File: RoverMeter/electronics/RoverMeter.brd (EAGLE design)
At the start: 35.6 x 14 mm, 17 parts, among them IC1 INA168, IC3 TINY85, J1 AVRISP, U1 MCP1824

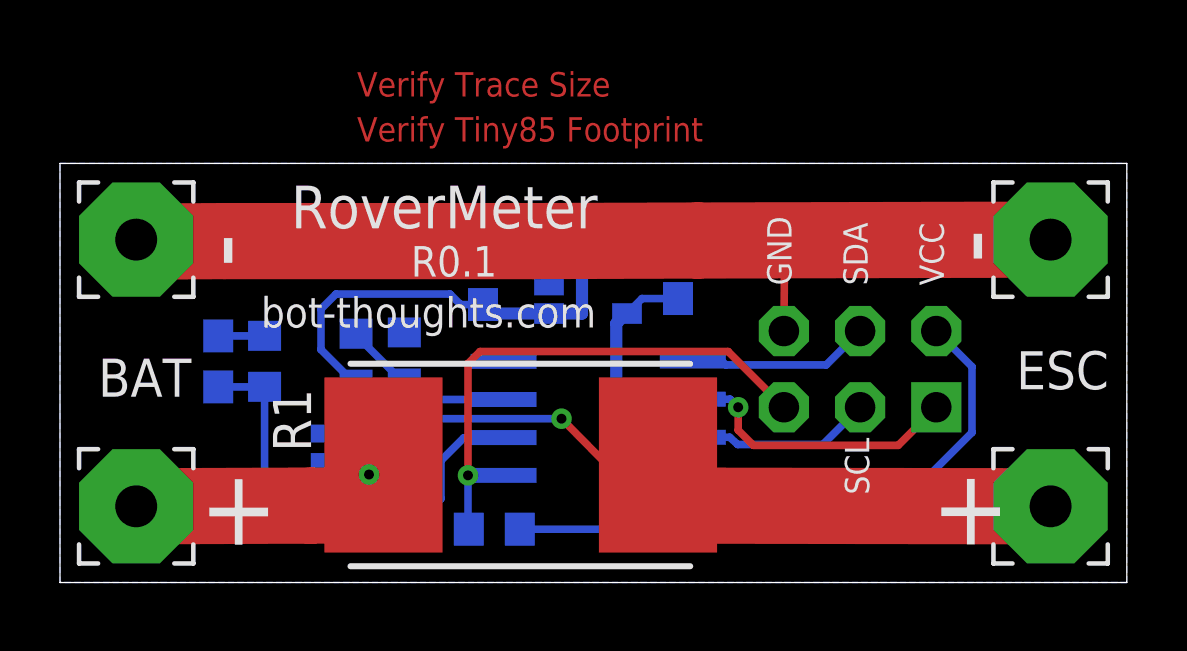
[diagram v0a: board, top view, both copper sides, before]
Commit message: Revised board layout somewhat
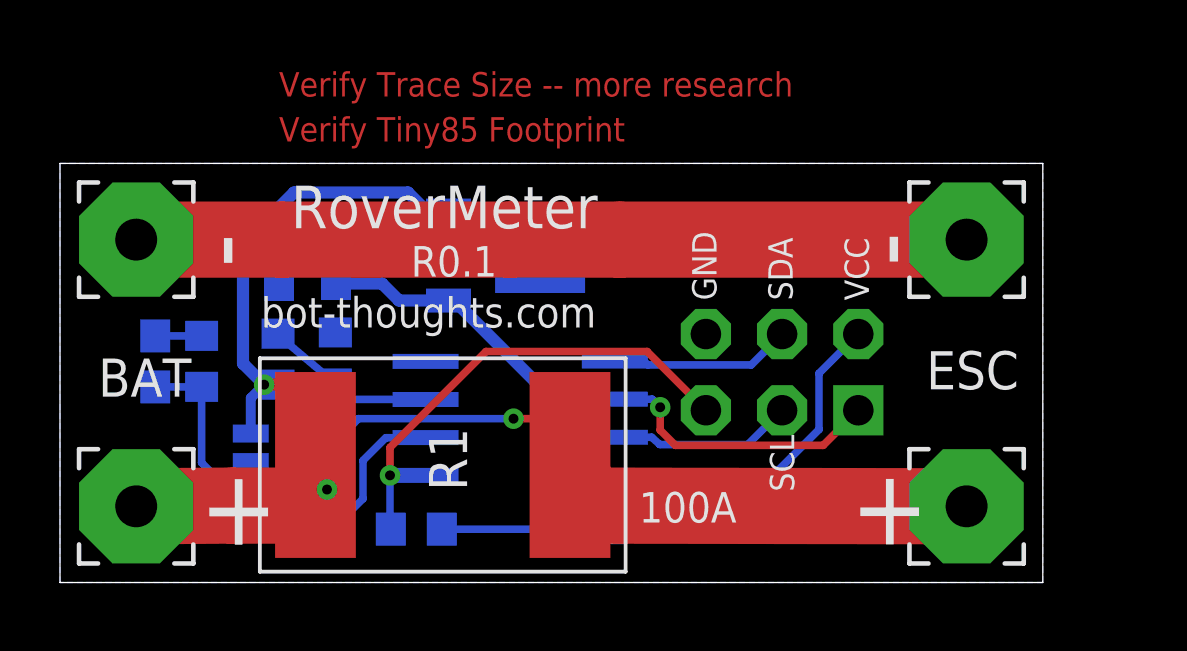
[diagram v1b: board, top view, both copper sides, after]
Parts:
- removed U1: MCP1824, bt_regulator:SOT23-5
- added IC2: KA78L05AIMTF, v-reg-3:SOT89
- R1: device rcl:R4527 -> bt:WSLP3921
- moved C3 11.4 mm to (9.20, 10.8)
- moved C4 6.83 mm to (7.30, 10.8), turned to 270 degrees
- moved PAD3 2.80 mm to (30.2, 2.54)
- moved PAD4 2.80 mm to (30.2, 11.4)
- moved J1 2.60 mm to (24.1, 7.01)
- moved IC1 2.60 mm to (7.67, 4.02)
- moved R3 2.60 mm to (7.27, 7.45)
- moved IC3 2.60 mm to (15.3, 5.48)
- moved R1 2.60 mm to (12.8, 3.92)
- moved R5 2.60 mm to (11.9, 1.78)
- moved C2 2.60 mm to (17.5, 1.78)
- moved R4 2.30 mm to (9.18, 7.49)
- moved C1 2.10 mm to (3.17, 7.37)
- moved R2 2.10 mm to (4.72, 7.37)
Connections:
- net 5V: now also IC2.1; no longer U1.5
- net GND: now also IC2.2; no longer U1.2
- net N$4: now also R1.P$2; no longer R1.2
- net V+: now also IC2.3, R1.P$1; no longer R1.1, U1.1, U1.3
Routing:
- net GND: track 38.1 -> 32.6 mm
- net V+: track 30.8 -> 28.3 mm, vias 1 -> 2
- net !RESET: track 18.2 -> 16.6 mm
- net 5V: track 29.0 -> 30.1 mm
- net AMP: track 14.8 -> 14.0 mm
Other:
- board size 35.6 x 14 mm -> 32.8 x 14 mm
- board text added: "100A"
- board text added: "Verify Trace Size -- more research"
- board text removed: "Verify Trace Size"
